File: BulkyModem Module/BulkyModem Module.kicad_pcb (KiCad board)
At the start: 2 copper layers, 100 x 100 mm, 80 parts, among them J1 DC IN, J2 DCE, J3 Module_Panel, J5 C64_Modem_IDC, K1 HK19F-DC, M1 Mounting, M2 Mounting, M3 Mounting, M4 Mounting, U1 74HCT244, U2 74HCT04, U3 MAX232, U4 MAX232, U5 74HCT04, U6 74HCT32

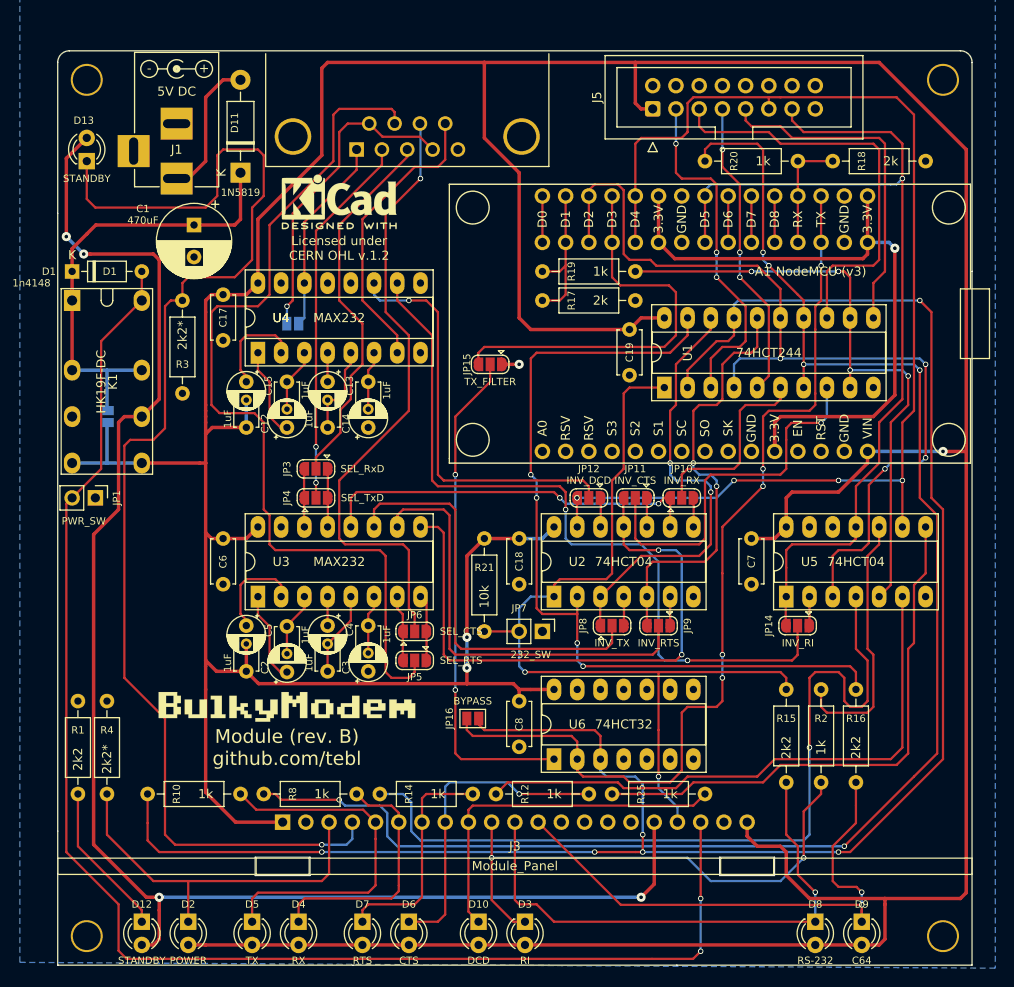
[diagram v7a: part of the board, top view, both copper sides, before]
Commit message: Revised version. Mainly buffering signals
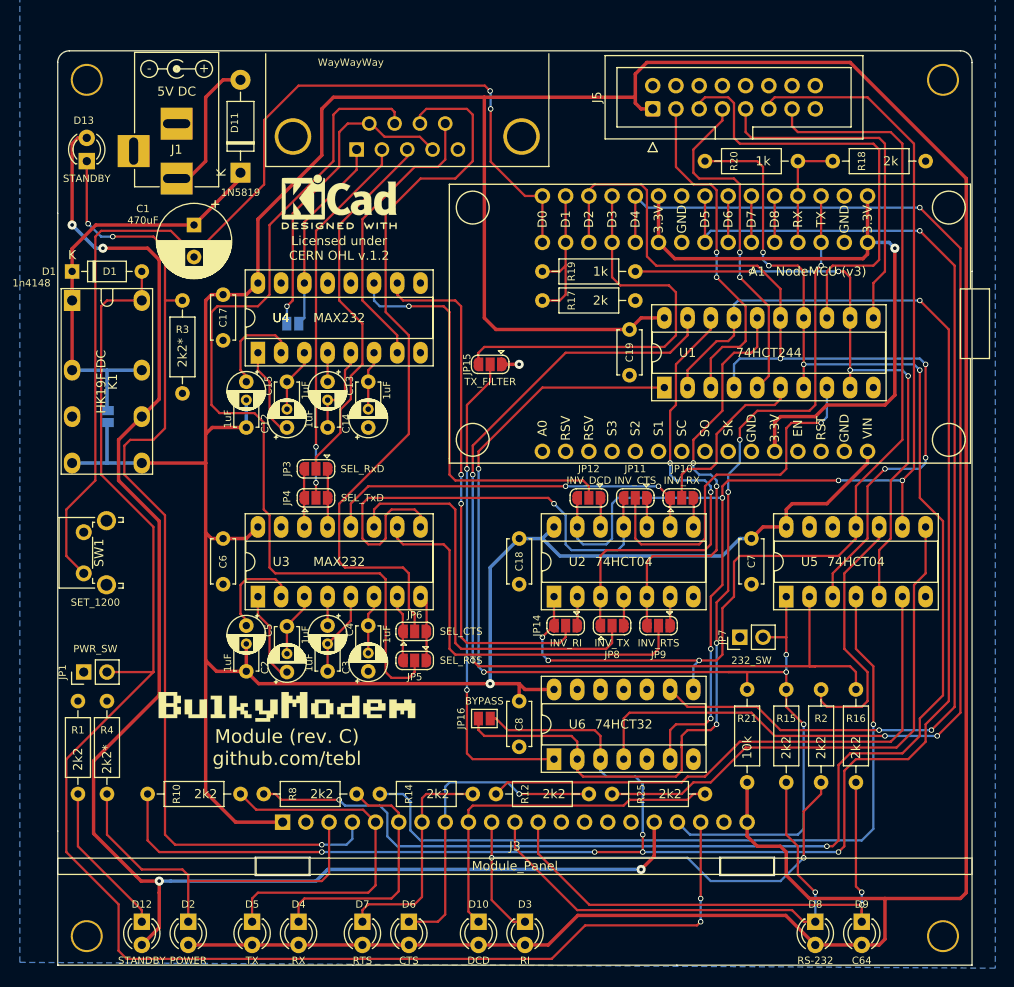
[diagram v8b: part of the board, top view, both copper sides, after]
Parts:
- added SW1: SET_1200, Button_Switch_THT:SW_Tactile_SPST_Angled_PTS645Vx39-2LFS, F.Cu at (73.0, 111.8)
- R10, R12, R14, R2, R25, R8: value 1k -> 2k2
- moved R21 29.4 mm to (145.6, 124.5), turned to 270 degrees
- moved JP14 25.4 mm to (125.7, 117.5)
- moved JP7 21.6 mm to (144.8, 118.7), turned to 90 degrees
- moved JP1 19.1 mm to (73.0, 122.6), turned to 90 degrees
- moved JP16 1.27 mm to (116.8, 127.6)
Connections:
- net Net-(A1-Pad21) renamed /ESP_DSR
- net Net-(A1-Pad22) renamed /ESP_DTR
- net Net-(A1-Pad27) renamed /TX_FILTER
- A1 pad 23: ESP_RI -> Net-(A1-Pad23)
- A1 pad 26: ESP_DCD -> Net-(A1-Pad26)
- U2 pad 1: MODE_232 -> ESP_RI
- U2 pad 2: MODE_C64 -> Net-(JP14-Pad1)
- U5 pad 1: ESP_RI -> MODE_232
- U5 pad 2: Net-(JP14-Pad1) -> MODE_C64
- U6 pad 4: GND -> Net-(A1-Pad26)
- U6 pad 6: (no net) -> ESP_DCD
- U6 pad 8: (no net) -> ESP_RI
- U6 pad 9: GND -> Net-(A1-Pad23)
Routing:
- net Net-(A1-Pad26): track 0.00 -> 137.4 mm, vias 0 -> 3
- net Net-(A1-Pad23): track 0.00 -> 117.1 mm, vias 0 -> 3
- net Net-(A1-Pad30): track 5.08 -> 114.4 mm, vias 0 -> 2
- net MODE_232: track 95.8 -> 128.1 mm, vias 2 -> 5
- net /Front panel/LED_STB: track 140.1 -> 110.7 mm, vias 1 -> 3
- net Net-(JP14-Pad2): track 83.7 -> 58.2 mm
- net MODE_C64: track 92.3 -> 106.5 mm, vias 4 -> 2
- net /RS-232/DCE_RTS: track 68.5 -> 81.3 mm, vias 1 -> 0
- net ESP_RI: track 103.9 -> 116.3 mm, vias 1 -> 3
- net Net-(JP11-Pad3): track 65.5 -> 53.4 mm, vias 2 -> 1
- net PWR_EN: track 158.6 -> 168.7 mm
- net +5V: track 548.3 -> 557.2 mm, vias 3 -> 1
- net ESP_DCD: track 132.5 -> 140.3 mm, vias 4 -> 5
- net Net-(R14-Pad1): track 90.3 -> 84.7 mm
- net /C64_RTS: track 33.1 -> 38.0 mm, vias 3 -> 2
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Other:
- board text added: "Module (rev. C) github.com/tebl"
- board text added: "WayWayWay"
- board text removed: "Module (rev. B) github.com/tebl"
